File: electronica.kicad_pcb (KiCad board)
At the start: 2 copper layers, 164.1 x 110.1 mm, 79 parts, among them J1 Conn_01x08, P12 Conn_01x03_Socket, P13 Conn_01x03_Socket, P14 Conn_01x03_Socket, P27 Conn_01x03_Socket, P3V317 Conn_01x02_Socket, P5V18 Conn_01x02_Socket, U1 ESP32-DevKitC, U4 ULN2003AID, U6 TSR_1-2433

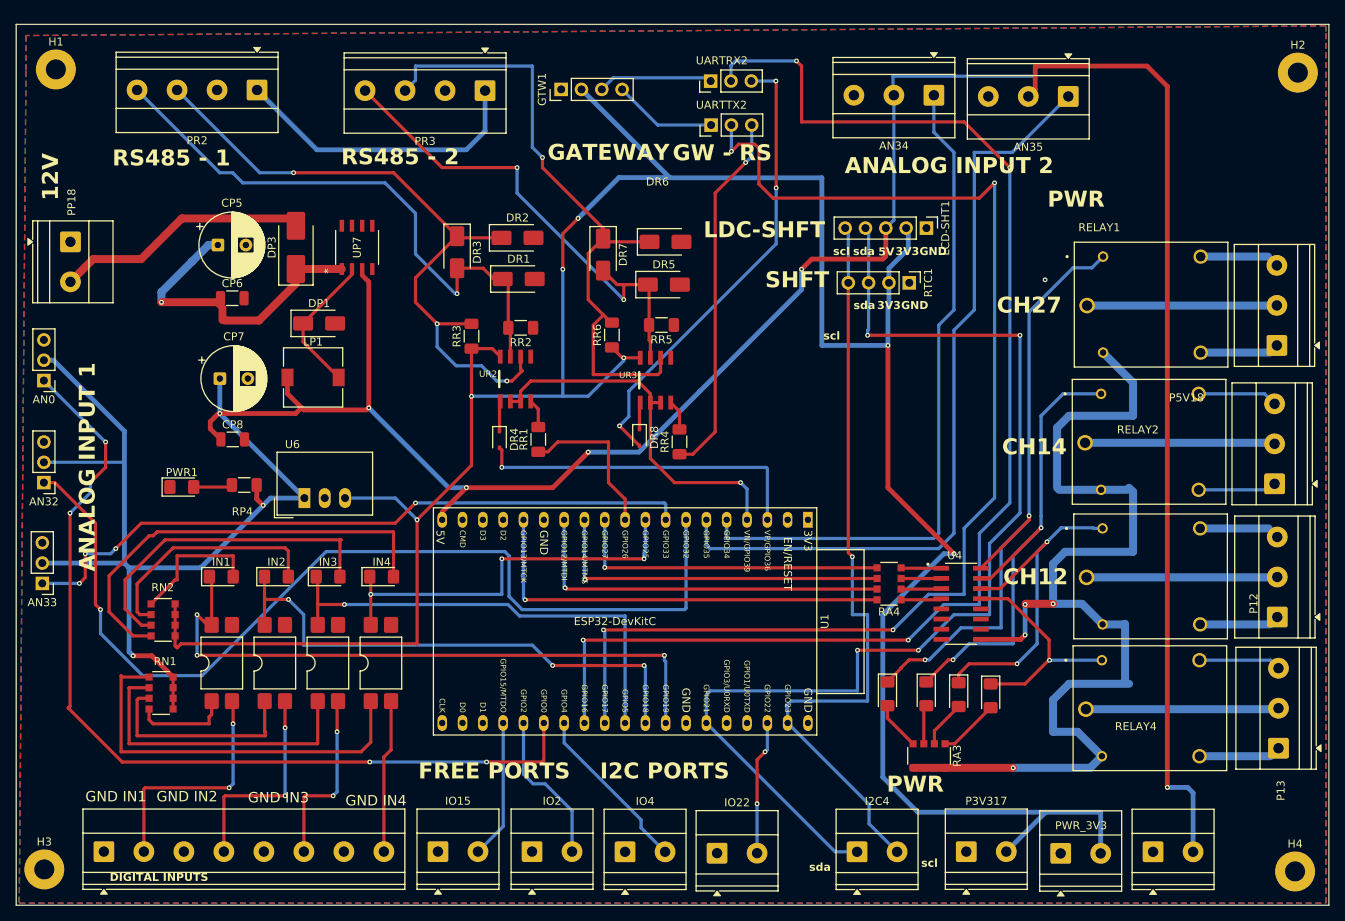
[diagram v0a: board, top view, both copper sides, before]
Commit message: agrege los foodprints de rtc, y shifter al pcb en general, agrege un par de pistas a los i2c de 3.3, los que trabajan a 5v los deje como sda-h  y sclh
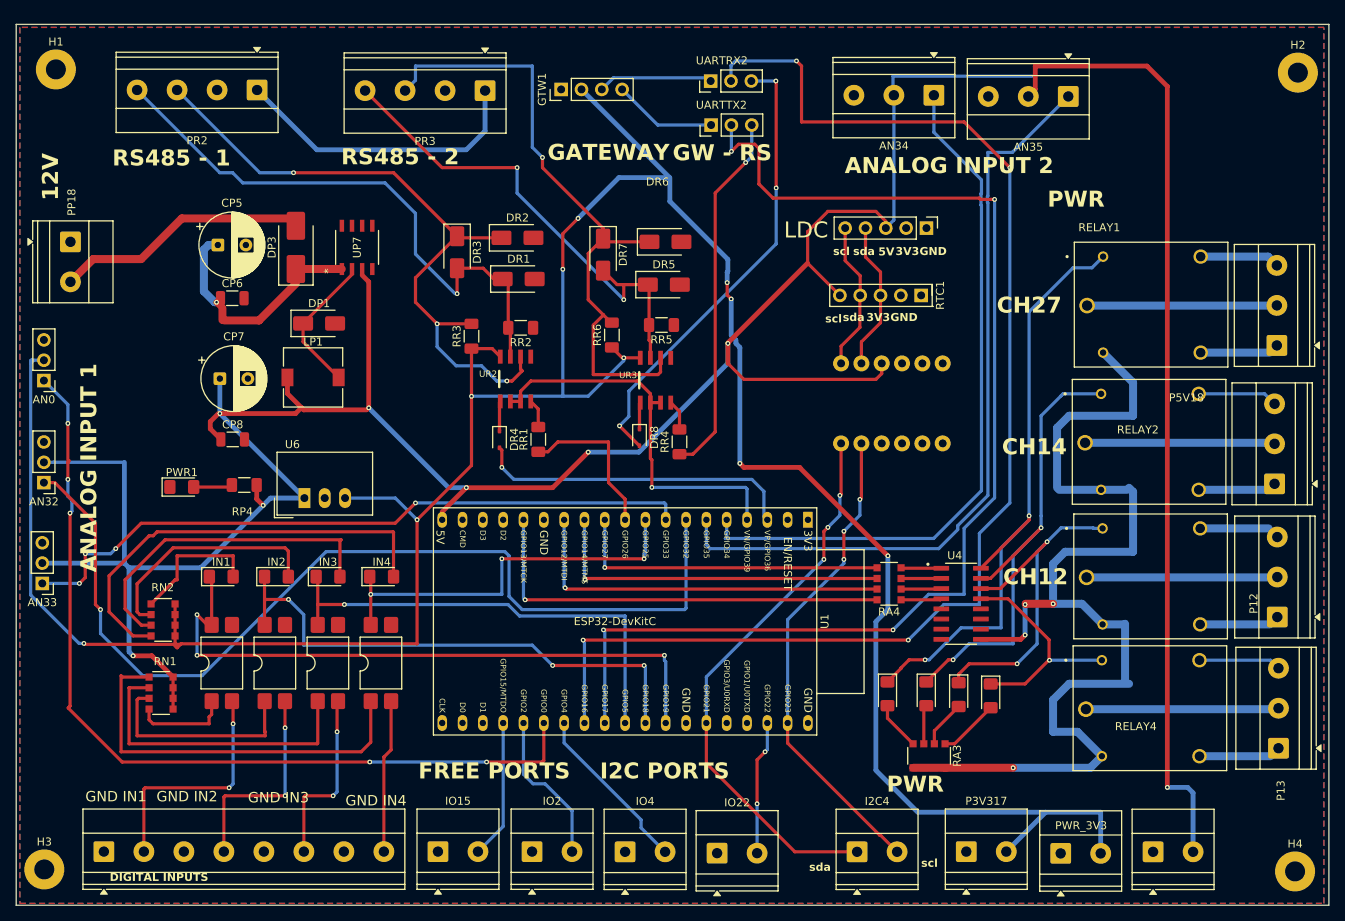
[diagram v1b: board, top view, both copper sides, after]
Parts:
- added shf4ch: Shifter4ch, Shifter4ch:Shifter4ch, F.Cu at (149.8, 84.7)
- moved RTC1 2.17 mm to (154.0, 71.2)
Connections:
- AN0 pad 2: 5V -> 3V3
- LCD-SHT1 pad 2: 3V3 -> (no net)
- LCD-SHT1 pad 4: IO21 -> SCL-H
- LCD-SHT1 pad 5: IO23 -> SDA-H
- RTC1 pad 2: 3V3 -> (no net)
- RTC1 pad 3: IO21 -> SCL-H
- RTC1 pad 4: IO23 -> SDA-H
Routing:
- net IO21: track 140.7 -> 70.4 mm, vias 4 -> 3
- net IO23: track 95.8 -> 60.6 mm, vias 1 -> 3
- net SDA-H: track 0.00 -> 19.2 mm
- net SCL-H: track 0.00 -> 18.7 mm
- net 3V3: track 334.2 -> 352.4 mm, vias 7 -> 10
- net 5V: track 417.5 -> 432.2 mm
- net /power/12V: track 39.3 -> 31.0 mm
- net IO0: track 113.1 -> 109.8 mm
- net IO34: track 85.9 -> 88.8 mm
- net IO17: track 154.4 -> 151.6 mm
- net IO39: track 46.8 -> 48.8 mm
- net IO36: track 42.2 -> 40.3 mm
- net IO35: track 98.4 -> 97.4 mm
- net GND: vias 1 -> 0
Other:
- board text added: "LDC"
- board text removed: "LDC-SHFT"
- board text removed: "SHFT"

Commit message: feat: integrated rtc ldc i2c / fixed 12v power line rs485 / output com pin -> input power type
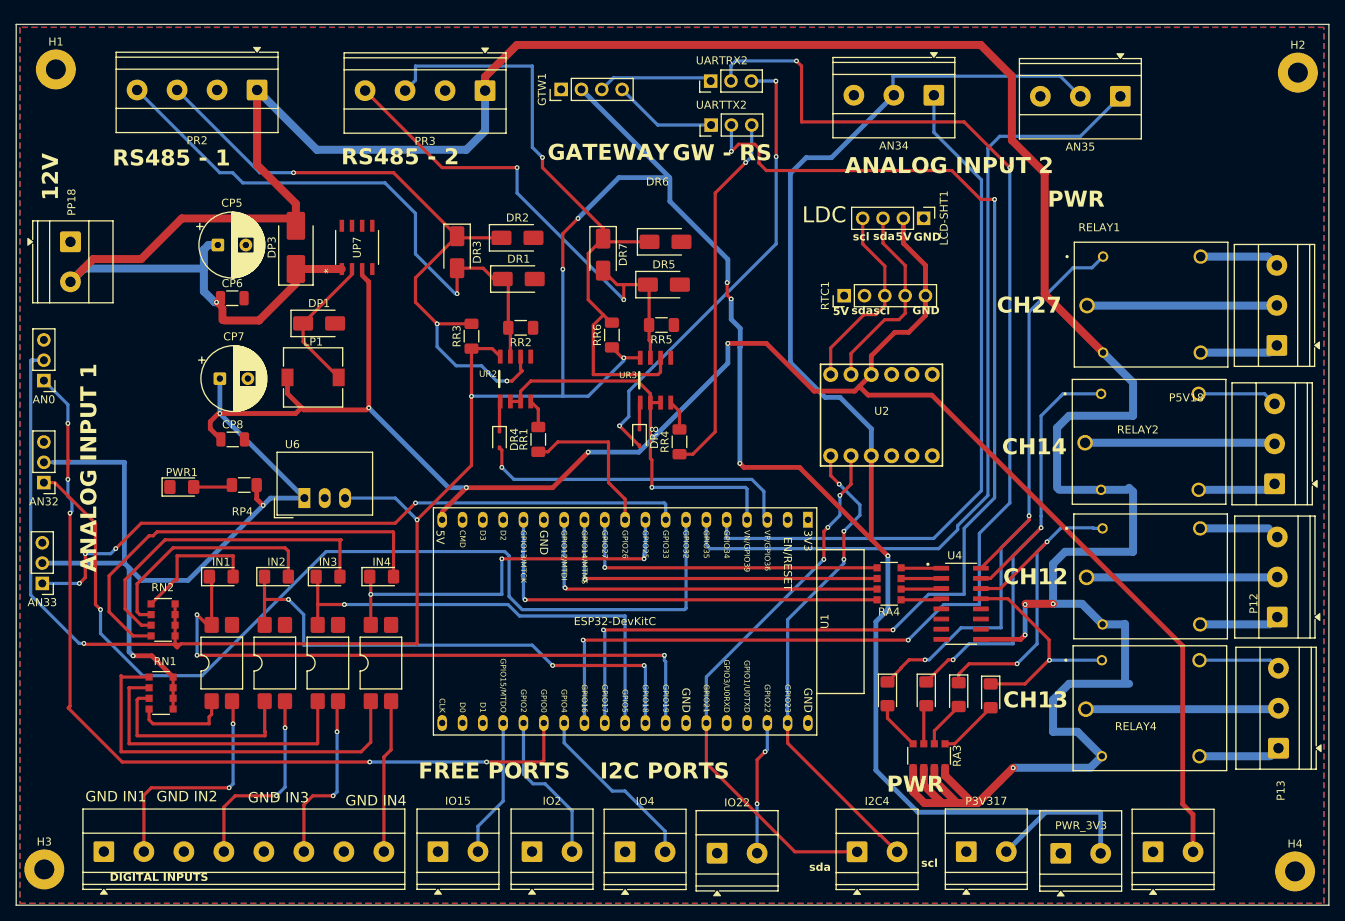
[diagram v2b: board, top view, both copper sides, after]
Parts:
- removed shf4ch: Shifter4ch, Shifter4ch:Shifter4ch
- added U2: ~, bioreactor_various:Level_Shifter_Bidir, F.Cu at (149.1, 86.2)
- LCD-SHT1: value Conn_01x05_Socket -> Conn_01x04_Socket; footprint Connector_PinHeader_2.54mm:PinHeader_1x05_P2.54mm_Vertical -> Connector_PinHeader_2.54mm:PinHeader_1x04_P2.54mm_Vertical
- RTC1: footprint Connector_PinHeader_2.54mm:PinHeader_1x04_P2.54mm_Vertical -> Connector_PinHeader_2.54mm:PinHeader_1x05_P2.54mm_Vertical
- moved RTC1 9.62 mm to (144.4, 71.3), turned to 90 degrees
- moved AN35 6.51 mm to (178.9, 46.3)
- moved LCD-SHT1 1.27 mm to (154.3, 61.6)
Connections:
- net SCL-H renamed /i2c/IO23H-SCL
- AN34 pad 2: 5V -> 3V3
- AN35 pad 2: 5V -> 3V3
- CP5 pad 1: /power/12V -> 12V
- CP6 pad 1: /power/12V -> 12V
- DP3 pad 1: /power/12V -> 12V
- DP3 pad 2: /power/VIN -> 12V
- LCD-SHT1 pad 2: (no net) -> 5V
- LCD-SHT1 pad 3: 5V -> /i2c/IO21H-SDA
- PP18 pad 2: /power/VIN -> 12V
- PR2 pad 1: /rs485/12V -> 12V
- PR3 pad 1: /rs485/12V -> 12V
- RTC1 pad 2: (no net) -> unconnected-(RTC1-Pin_2-Pad2)
- RTC1 pad 4: SDA-H -> /i2c/IO21H-SDA
- UP7 pad 1: /power/12V -> 12V
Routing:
- net 12V: track 136.8 -> 405.7 mm, vias 4 -> 5
- net 3V3: track 352.4 -> 450.3 mm
- net 5V: track 432.2 -> 339.0 mm, vias 8 -> 7
- net /rs485/12V: track 37.6 -> 0.00 mm
- net /power/VIN: track 31.8 -> 0.00 mm
- net /power/12V: track 31.0 -> 0.00 mm, vias 1 -> 0
- net /i2c/IO21H-SDA: track 0.00 -> 24.5 mm
- net SDA-H: track 19.2 -> 0.00 mm
- net IO35: track 97.4 -> 104.2 mm
- net /i2c/IO23H-SCL: track 18.7 -> 24.3 mm
- net IO17: track 151.6 -> 150.1 mm
- net IN2: track 26.4 -> 25.0 mm
- net IO21: track 70.4 -> 69.4 mm
- net IO4: track 21.3 -> 22.2 mm
- net IN3: track 22.6 -> 22.1 mm
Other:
- board text added: "CH13"
- board text removed: "3V3"

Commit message: draft:updating pcb dimentions
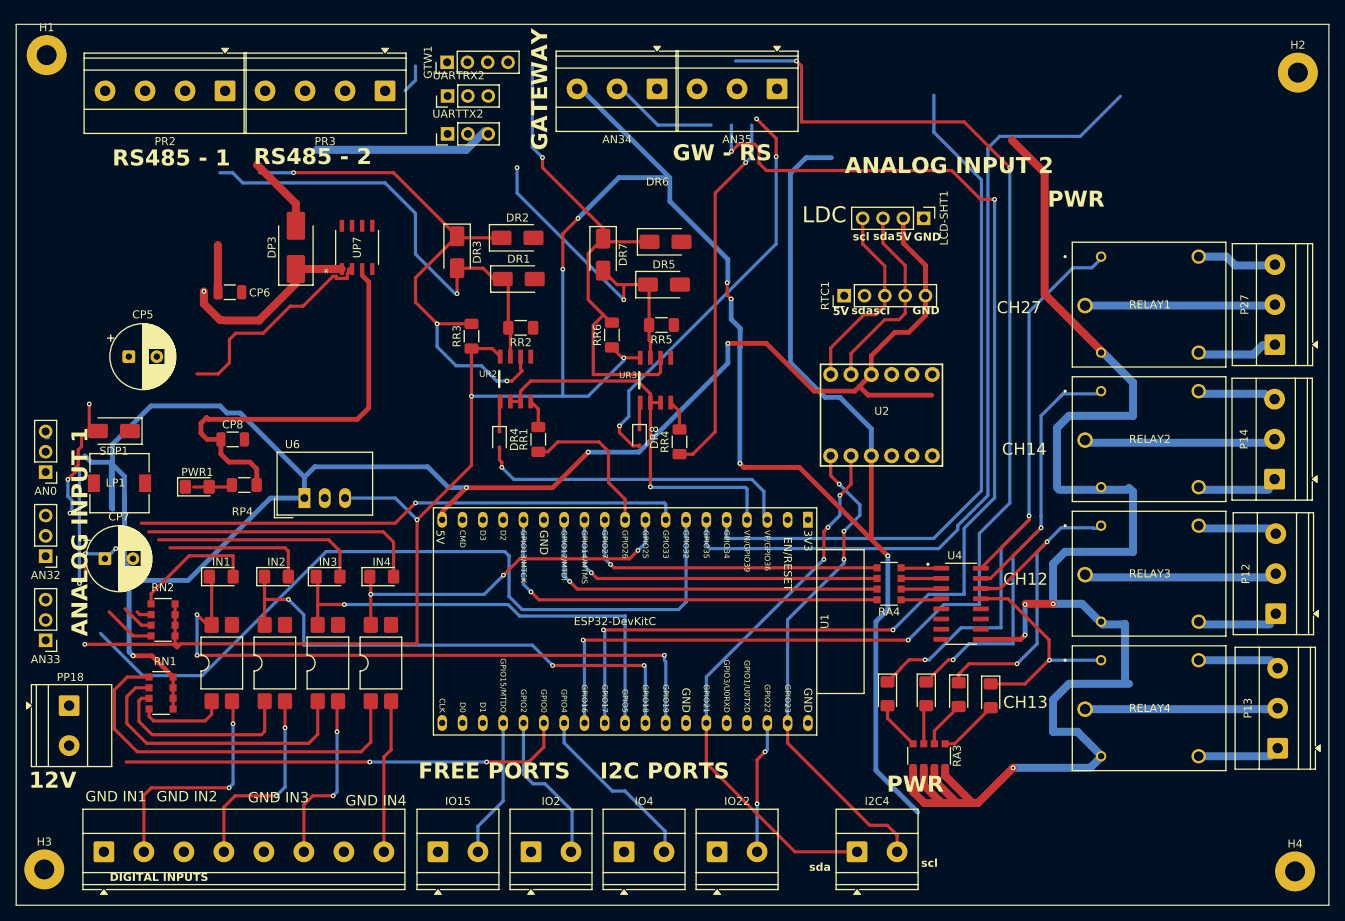
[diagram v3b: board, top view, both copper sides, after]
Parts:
- removed P3V317, P5V18, PWR_3V3: Conn_01x02_Socket, TerminalBlock_Phoenix:TerminalBlock_Phoenix_MKDS-1,5-2_1x02_P5.00mm_Horizontal
- moved PP18 58.0 mm to (47.5, 122.5)
- moved AN35 42.9 mm to (136.0, 45.4)
- moved AN34 34.6 mm to (121.0, 45.4)
- moved UARTTX2 33.0 mm to (94.8, 51.0)
- moved UARTRX2 32.9 mm to (94.8, 46.3)
- moved SDP1 29.0 mm to (53.1, 88.2), turned to 180 degrees
- moved LP1 27.6 mm to (53.8, 94.7)
- moved CP7 26.7 mm to (52.0, 104.1)
- moved CP5 17.9 mm to (55.0, 78.9)
- moved GTW1 14.7 mm to (94.8, 42.1)
- moved PR3 12.5 mm to (87.0, 45.7)
- moved AN0 11.4 mm to (44.6, 93.3)
- moved AN32 9.20 mm to (44.6, 103.8)
- moved AN33 7.12 mm to (44.6, 114.3)
- moved PR2 4.00 mm to (67.0, 45.7)
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- renumbered DP1 to SDP1
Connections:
- AN0 pad 2: 3V3 -> 5V
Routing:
- net 12V: track 405.7 -> 232.8 mm
- net 3V3: track 450.3 -> 350.7 mm
- net IO0: track 109.8 -> 56.0 mm, vias 5 -> 2
- net IO32: track 121.5 -> 98.5 mm, vias 1 -> 0
- net /rs485/B2-: track 62.5 -> 39.5 mm
- net 5V: track 339.0 -> 320.2 mm
- net /rs485/A2+: track 80.3 -> 62.1 mm
- net IO33: track 85.9 -> 68.6 mm, vias 4 -> 1
- net GND: track 0.00 -> 15.9 mm, vias 0 -> 3
- net /rs485/RO: track 58.0 -> 73.7 mm
- net /rs485/B1-: track 73.1 -> 58.4 mm
- net /rs485/A1+: track 84.4 -> 69.8 mm
- net /rs485/RX: track 14.4 -> 0.00 mm
- net /rs485/TX: track 13.0 -> 0.00 mm
- net Net-(IN4-A): track 54.4 -> 42.0 mm
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- removed copper zone on B.Cu, net GND
- removed copper zone on F.Cu, net GND
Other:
- board text added: "GPIO14/MTMS"

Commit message: feat: position of the components improved
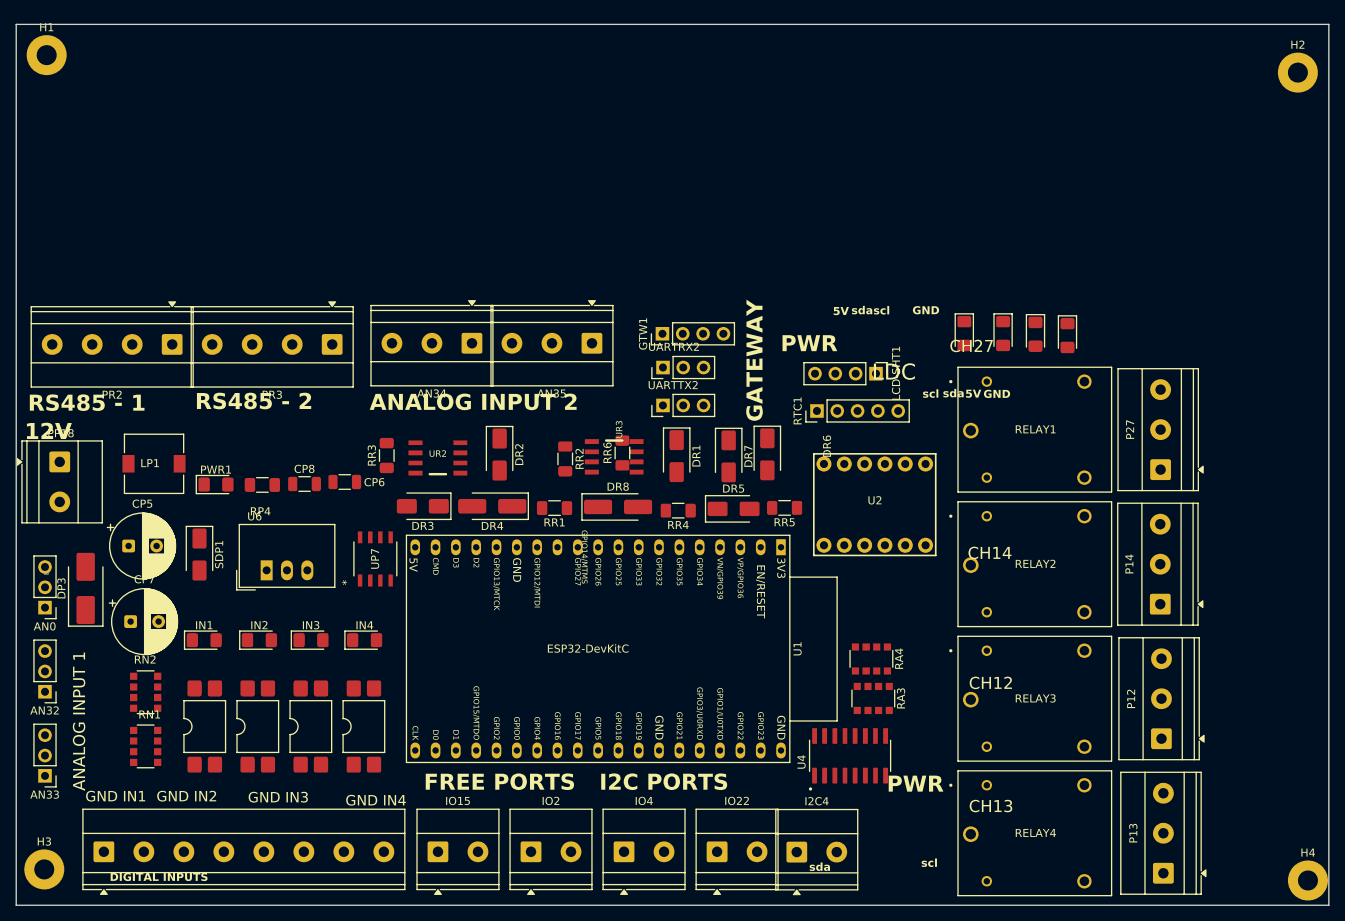
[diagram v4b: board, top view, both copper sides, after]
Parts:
- DR4, DR8: footprint Diode_SMD:D_SOD-323 -> Diode_SMD:D_SMA_Handsoldering
- moved DP3 50.1 mm to (49.6, 107.9)
- moved CH3 46.0 mm to (168.3, 76.1)
- moved CH4 46.0 mm to (172.3, 76.2)
- moved CH1 46.0 mm to (159.4, 76.0)
- moved CH2 46.0 mm to (164.2, 76.0)
- moved GTW1 43.3 mm to (121.7, 76.0)
- moved UARTRX2 43.3 mm to (121.7, 80.2)
- moved UARTTX2 43.3 mm to (121.7, 85.0)
- moved AN34 39.3 mm to (97.9, 77.2)
- moved AN35 39.3 mm to (112.9, 77.2)
- moved UP7 39.0 mm to (85.8, 104.2)
- moved PR2 32.4 mm to (60.4, 77.4)
- moved PR3 32.4 mm to (80.4, 77.4)
- moved DR3 32.0 mm to (91.7, 97.6), turned to 180 degrees
- moved PP18 30.5 mm to (46.3, 92.0)
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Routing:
- net 3V3: track 350.7 -> 0.00 mm, vias 10 -> 0
- net 5V: track 320.2 -> 0.00 mm, vias 7 -> 0
- net 12V: track 232.8 -> 0.00 mm, vias 5 -> 0
- net IO16: track 161.9 -> 0.00 mm, vias 4 -> 0
- net IO17: track 150.1 -> 0.00 mm, vias 4 -> 0
- net IO35: track 104.2 -> 0.00 mm
- net IO32: track 98.5 -> 0.00 mm
- net IO34: track 88.8 -> 0.00 mm
- net IO19: track 80.5 -> 0.00 mm, vias 3 -> 0
- net OUT1: track 79.1 -> 0.00 mm, vias 2 -> 0
- net /rs485/RO: track 73.7 -> 0.00 mm, vias 3 -> 0
- net /rs485/A1+: track 69.8 -> 0.00 mm, vias 3 -> 0
- net IO21: track 69.4 -> 0.00 mm, vias 3 -> 0
- net IO33: track 68.6 -> 0.00 mm, vias 1 -> 0
- net IO18: track 66.4 -> 0.00 mm, vias 3 -> 0
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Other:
- board text removed: "GW - RS"
